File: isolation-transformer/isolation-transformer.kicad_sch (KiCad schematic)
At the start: 36 parts, among them J1 Conn_BNC_Vert_PCB, J2 Conn_BNC_Vert_PCB, J3 Conn_BNC_Vert_PCB, J4 Conn_BNC_Vert_PCB, T1 Hammond_560, T2 Hammond_560

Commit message: feat: routing of iso-xfmr complete
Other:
- company: (none) -> ©2024 Winry Litwa-Vulcu
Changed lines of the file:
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@@
 		(date "2024-04-22")
 		(rev "A0")
+		(company "©2024 Winry Litwa-Vulcu")
+		(comment 1 "Drawn By: Winry Litwa-Vulcu")
+		(comment 2 "Designed By: Winry Litwa-Vulcu")
+		(comment 4 "github.com/vulcu")
 	)
 	(junction

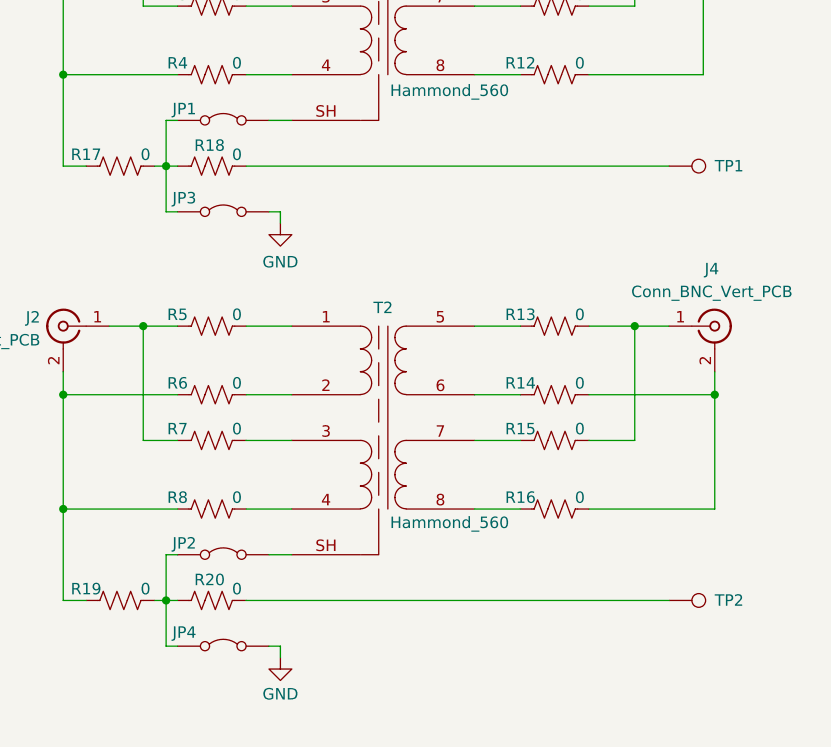
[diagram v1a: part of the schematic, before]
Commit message: feat: add bypass caps to GND connection
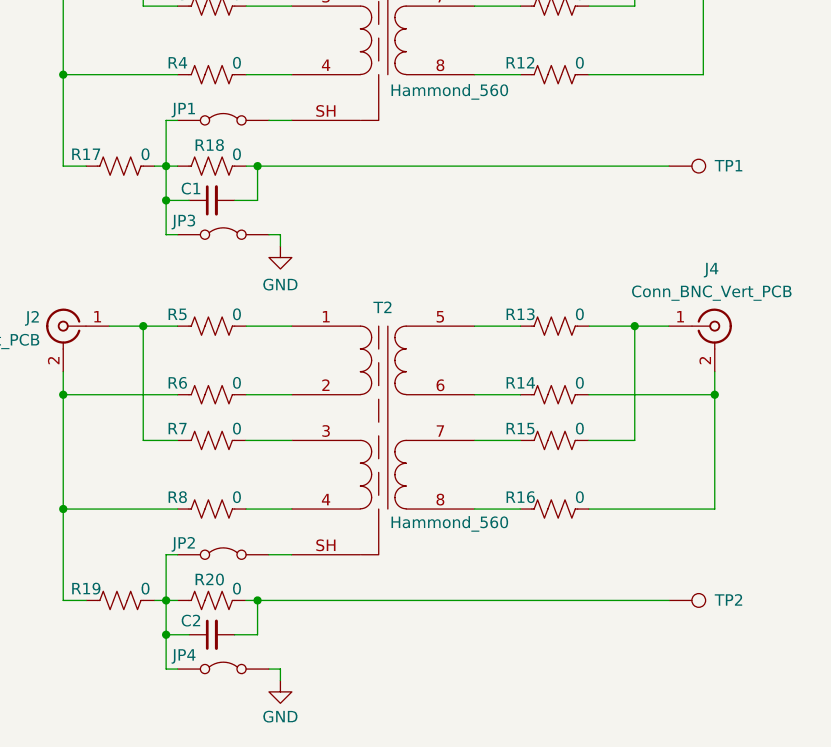
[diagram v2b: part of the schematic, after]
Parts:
- added C1, C2: C_Small, Capacitor_SMD:C_0603_1608Metric_Pad1.08x0.95mm_HandSolder, symbol Device:C_Small
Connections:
- net at JP2.1 (A), JP4.1 (A), R19.2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: now also C2.1
- net at JP1.1 (A), JP3.1 (A), R17.2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: now also C1.1
- net at R18.2, TP1.1: now also C1.2
- net at R20.2, TP2.1: now also C2.2
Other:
- moved on the sheet: JP3, JP4

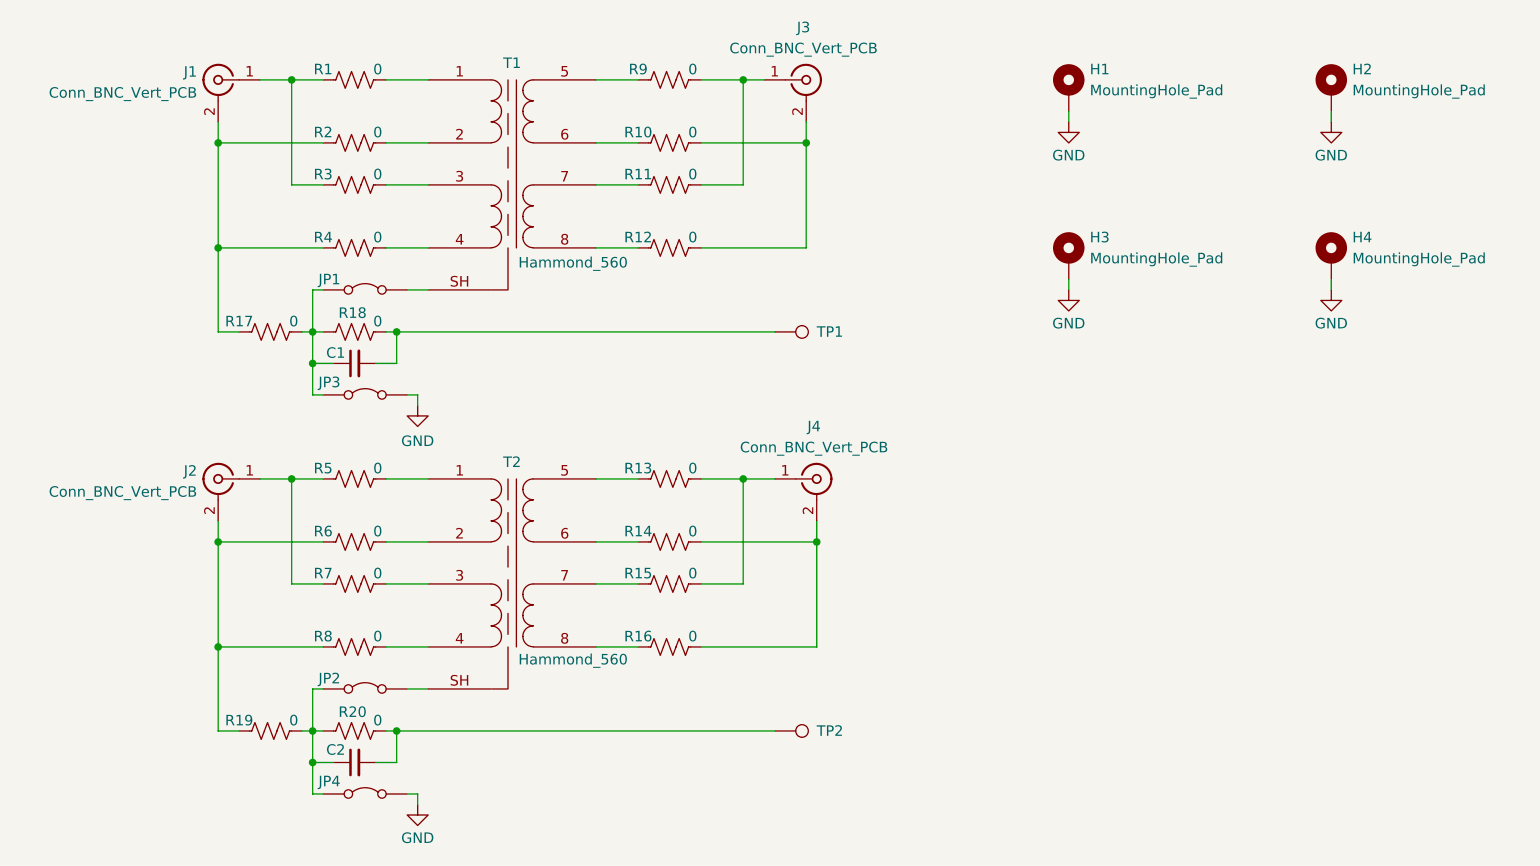
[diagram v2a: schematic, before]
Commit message: fix (PCB): zero-ohm resistor alignment mismatch between in/out
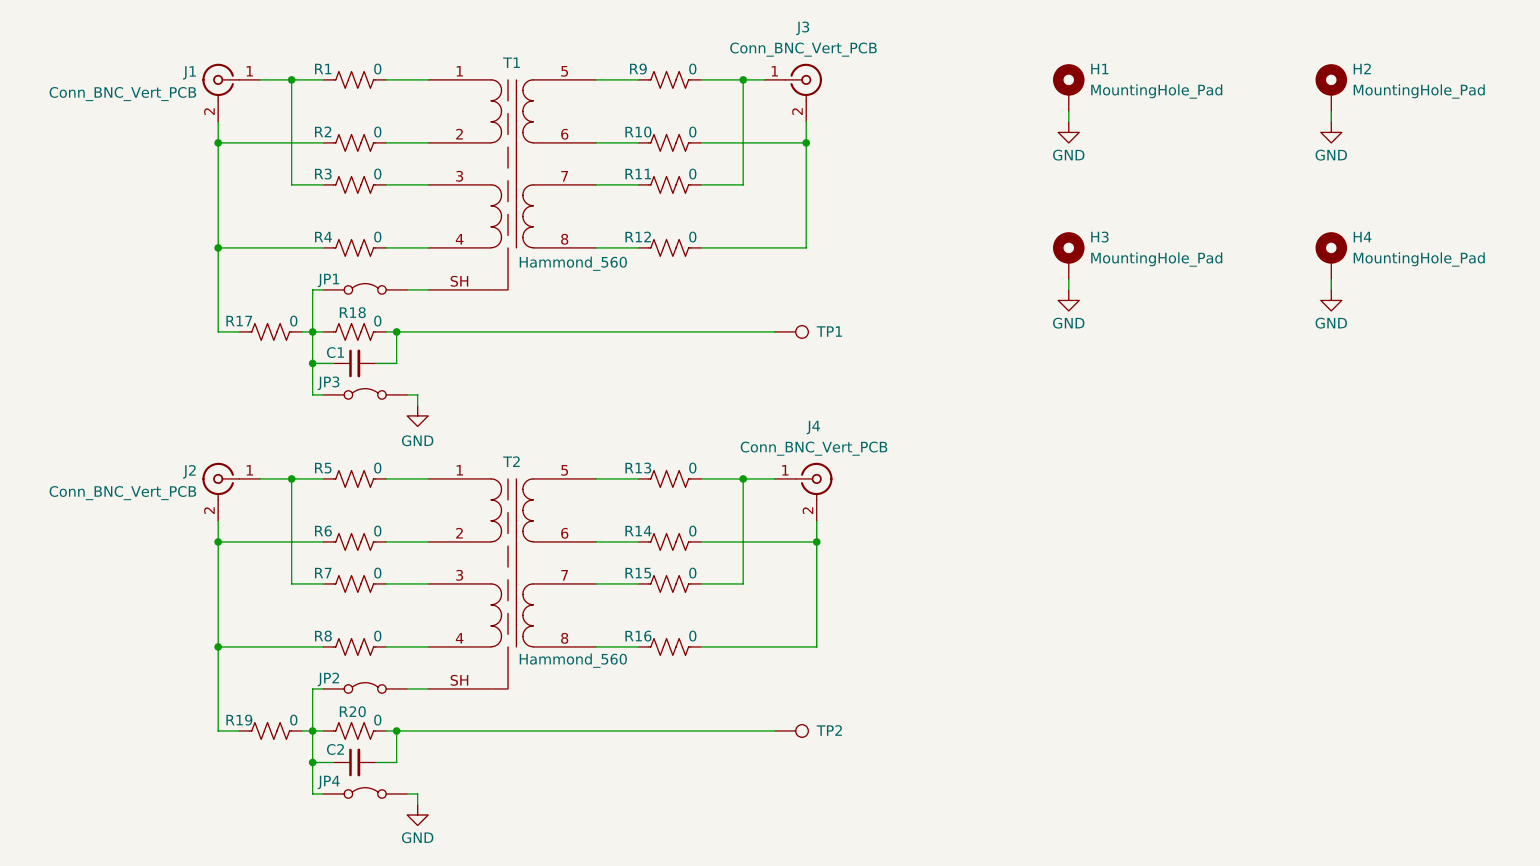
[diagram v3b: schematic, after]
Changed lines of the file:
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@@
 (kicad_sch
-	(version 20231120)
+	(version 20250114)
 	(generator "eeschema")
-	(generator_version "8.0")
+	(generator_version "9.0")
 	(paper "A4")
 	(title_block
@@
 		)
 	)
+	(embedded_fonts no)
 )
